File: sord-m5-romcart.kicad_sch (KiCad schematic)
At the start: 1 part

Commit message: Investigating banking
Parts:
- added U2: 27C256, Package_DIP:DIP-28_W15.24mm, symbol Memory_EPROM:27C256
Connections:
- net +5V: now also U2.28 (VCC)
- net GND: now also U2.1 (VPP), U2.14 (GND)
- net D1: now reaches U1.10 (D1)
- net D1: now also U2.12 (D1)
- net D0: now reaches U1.11 (D0)
- net D0: now also U2.11 (D0)
- net A7: now reaches U1.12 (A7)
- net A7: now also U2.3 (A7)
- net A6: now reaches U1.13 (A6)
- net A6: now also U2.4 (A6)
- net A5: now reaches U1.14 (A5)
- net A5: now also U2.5 (A5)
- net A4: now reaches U1.15 (A4)
- net A4: now also U2.6 (A4)
- net A3: now reaches U1.16 (A3)
- net A3: now also U2.7 (A3)
- net A2: now reaches U1.17 (A2)
- net A2: now also U2.8 (A2)
- net A1: now reaches U1.18 (A1)
- net A1: now also U2.9 (A1)
- net A0: now reaches U1.19 (A0)
- net A0: now also U2.10 (A0)
- net ~{ROM0}: now reaches U1.22 (~{ROM0})
- net ~{ROM0}: now also U2.20 (~{CE})
- net ~{MEM_RD}: now reaches U1.24 (~{MEM_RD})
- net ~{MEM_RD}: now also U2.22 (~{OE})
- net D4: now reaches U1.36 (D4)
- net D4: now also U2.16 (D4)
- net D5: now reaches U1.37 (D5)
- net D5: now also U2.17 (D5)
- net D6: now reaches U1.38 (D6)
- net D6: now also U2.18 (D6)
- net D7: now reaches U1.39 (D7)
- net D7: now also U2.19 (D7)
- net A8: now reaches U1.40 (A8)
- net A8: now also U2.25 (A8)
- net A9: now reaches U1.41 (A9)
- net A9: now also U2.24 (A9)
- net A10: now reaches U1.42 (A10)
- net A10: now also U2.21 (A10)
- net A11: now reaches U1.43 (A11)
- net A11: now also U2.23 (A11)
- net A12: now reaches U1.44 (A12)
- net D3: now reaches U1.8 (D3)
- net D3: now also U2.15 (D3)
- net D2: now reaches U1.9 (D2)
- net D2: now also U2.13 (D2)
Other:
- note added: "0x2000 (A13)"
- note added: "0x4000"
- note added: "0x6000"
- note added: "BASIC-{F,G,I,W}?"
- note added: "TODO: BASIC-G cartridge also needs RAM (http://www.retropc.net/mm/m5/basic-g-logic.html)"
- note added: "TODO: BASIC-G is 16K + RAM, BASIC-I is 8K"
- note added: "TODO: Do a table and figure out where each ROM select is at (add a 139?)"

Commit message: Fumbling
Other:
- note added: "0x4000 (A14)"
- note added: "0x6000 (A13 + A14, "only 4k")"
- note removed: "0x4000"
- note removed: "0x6000"
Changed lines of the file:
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@@
 	(text "0x2000 (A13)"
 		(exclude_from_sim no)
-		(at 122.555 67.31 0)
+		(at 116.205 67.31 0)
 		(effects
 			(font
 				(size 1.27 1.27)
 			)
+			(justify left)
 		)
 	)
-	(text "0x6000"
+	(text "0x6000 (A13 + A14, \"only 4k\")"
 		(exclude_from_sim no)
-		(at 119.38 72.39 0)
+		(at 116.205 72.39 0)
 		(effects
 			(font
 				(size 1.27 1.27)
 			)
+			(justify left)
 		)
 	)
@@
 		)
 	)
-	(text "0x4000"
+	(text "0x4000 (A14)"
 		(exclude_from_sim no)
-		(at 119.38 69.85 0)
+		(at 116.205 69.85 0)
 		(effects
 			(font
 				(size 1.27 1.27)
 			)
+			(justify left)
 		)
 	)

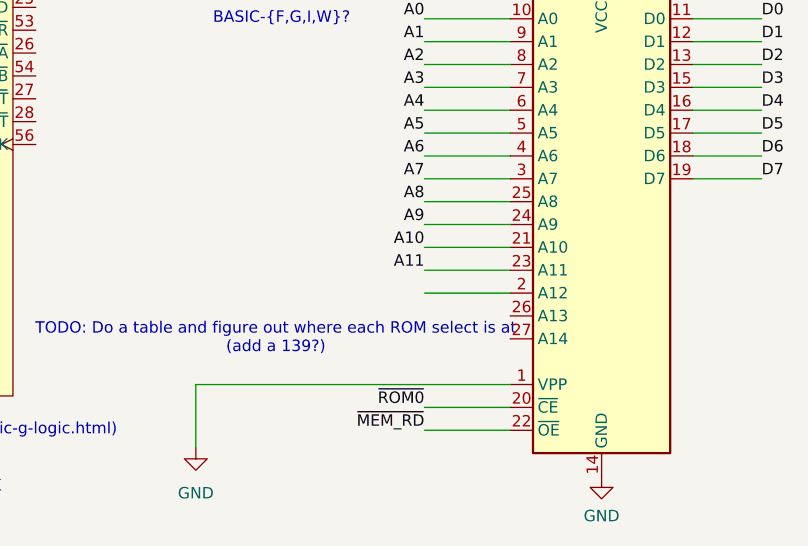
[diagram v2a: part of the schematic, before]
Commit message: A12 restored
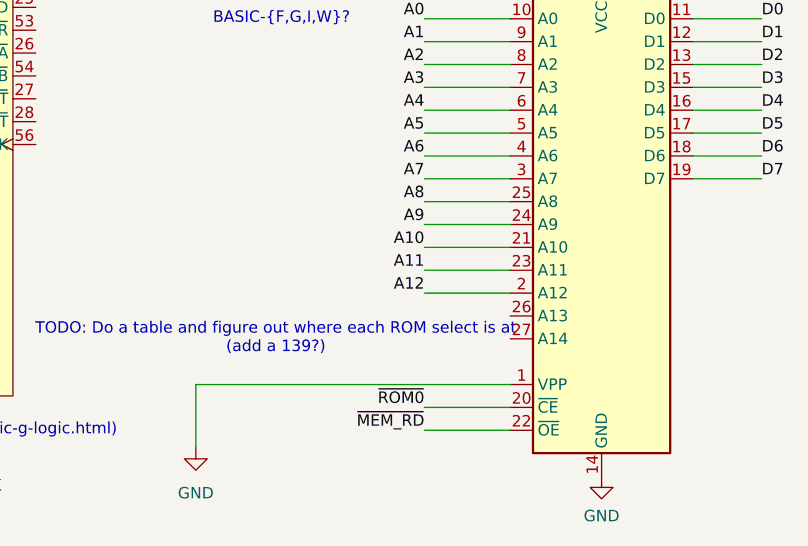
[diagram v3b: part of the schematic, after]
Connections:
- net A12: now also U2.2 (A12)
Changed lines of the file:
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@@
+		)
+	)
+	(label "A12"
+		(at 146.685 114.935 180)
+		(fields_autoplaced yes)
+		(effects
+			(font
+				(size 1.27 1.27)
+			)
+			(justify right bottom)
 		)
 	)

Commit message: Updated decode
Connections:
- net ~{ROM1}: now reaches U1.50 (~{ROM1})
- no-connect marks 0 -> 7
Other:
- note added: "TODO: decode the ROM0/ROM1 selects into high address lines"
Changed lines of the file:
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@@
 		(color 0 0 0 0)
 	)
+	(no_connect
+		(at 103.505 90.805)
+	)
+	(no_connect
+		(at 103.505 98.425)
+	)
+	(no_connect
+		(at 103.505 88.265)
+	)
+	(no_connect
+		(at 103.505 85.725)
+	)
+	(no_connect
+		(at 103.505 83.185)
+	)
+	(no_connect
+		(at 103.505 95.885)
+	)
+	(no_connect
+		(at 103.505 93.345)
+	)
 	(wire
 		(pts
@@
 		(pts
 			(xy 103.505 78.105) (xy 107.95 78.105)
+		)
+		(stroke
+			(width 0)
+			(type default)
+		)
+	)
+	(wire
+		(pts
+			(xy 103.505 70.485) (xy 107.95 70.485)
 		)
 		(stroke
@@
 		)
 	)
+	(text "TODO: decode the ROM0/ROM1 selects into high address lines"
+		(exclude_from_sim no)
+		(at 140.335 142.24 0)
+		(effects
+			(font
+				(size 1.27 1.27)
+			)
+		)
+	)
 	(label "A2"
 		(at 71.755 90.805 180)
@@
 		)
 	)
+	(label "~{ROM1}"
+		(at 107.95 70.485 0)
+		(fields_autoplaced yes)
+		(effects
+			(font
+				(size 1.27 1.27)
+			)
+			(justify left bottom)
+		)
+	)

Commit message: Board outline
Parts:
- U1: footprint (none) -> Sord:M5_CartridgeSlot
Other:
- note added: "TODO: Fix symbol pinout to be A/B"
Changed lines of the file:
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@@
+		)
+	)
+	(text "TODO: Fix symbol pinout to be A/B "
+		(exclude_from_sim no)
+		(at 76.835 144.78 0)
+		(effects
+			(font
+				(size 1.27 1.27)
+			)
 		)
 	)
@@
 			)
 		)
-		(property "Footprint" ""
+		(property "Footprint" "Sord:M5_CartridgeSlot"
 			(at 93.345 37.465 0)
 			(effects
@@
 			(at 93.345 37.465 0)
 			(effects
+				(font
+					(size 1.27 1.27)
+				)
+				(hide yes)
+			)
+		)
+		(property "DigiKey" ""
+			(at 93.345 37.465 0)
+			(effects

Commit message: Symbol cleanout
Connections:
- net +12V: now also U1.A2 (+12V_In), U1.A3 (+12V), U1.B2 (+12V_In), U1.B3 (+12V); no longer U1.2 (+12V_In), U1.3 (+12V), U1.30 (+12V_In), U1.31 (+12V)
- net +5V: now also U1.A4 (+5V_In), U1.A5 (+5V), U1.B4 (+5V_In), U1.B5 (+5V); no longer U1.32 (+5V_In), U1.33 (+5V), U1.4 (+5V_In), U1.5 (+5V)
- net -12V: now also U1.A1 (-12V), U1.B1 (-12V); no longer U1.1 (-12V), U1.29 (-12V)
- net A0: now also U1.A19 (A0); no longer U1.19 (A0)
- net A1: now also U1.A18 (A1); no longer U1.18 (A1)
- net A10: now also U1.B14 (A10); no longer U1.42 (A10)
- net A11: now also U1.B15 (A11); no longer U1.43 (A11)
- net A12: now also U1.B16 (A12); no longer U1.44 (A12)
- net A2: now also U1.A17 (A2); no longer U1.17 (A2)
- net A3: now also U1.A16 (A3); no longer U1.16 (A3)
- net A4: now also U1.A15 (A4); no longer U1.15 (A4)
- net A5: now also U1.A14 (A5); no longer U1.14 (A5)
- net A6: now also U1.A13 (A6); no longer U1.13 (A6)
- net A7: now also U1.A12 (A7); no longer U1.12 (A7)
- net A8: now also U1.B12 (A8); no longer U1.40 (A8)
- net A9: now also U1.B13 (A9); no longer U1.41 (A9)
- net D0: now also U1.A11 (D0); no longer U1.11 (D0)
- net D1: now also U1.A10 (D1); no longer U1.10 (D1)
- net D2: now also U1.A9 (D2); no longer U1.9 (D2)
- net D3: now also U1.A8 (D3); no longer U1.8 (D3)
- net D4: now also U1.B8 (D4); no longer U1.36 (D4)
- net D5: now also U1.B9 (D5); no longer U1.37 (D5)
- net D6: now also U1.B10 (D6); no longer U1.38 (D6)
- net D7: now also U1.B11 (D7); no longer U1.39 (D7)
- net GND: now also U1.A6 (GND), U1.A7 (GND), U1.B6 (GND), U1.B7 (GND); no longer U1.34 (GND), U1.35 (GND), U1.6 (GND), U1.7 (GND)
- net ~{MEM_RD}: now also U1.A24 (~{MEM_RD}); no longer U1.24 (~{MEM_RD})
- net ~{ROM0}: now also U1.A22 (~{ROM0}); no longer U1.22 (~{ROM0})
- net ~{ROM1}: now also U1.B22 (~{ROM1}); no longer U1.50 (~{ROM1})
- no-connect marks 7 -> 10
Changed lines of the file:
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@@
 	)
 	(no_connect
-		(at 103.505 98.425)
+		(at 103.505 100.965)
+	)
+	(no_connect
+		(at 103.505 103.505)
+	)
+	(no_connect
+		(at 103.505 108.585)
+	)
+	(no_connect
+		(at 103.505 106.045)
 	)
 	(no_connect
@@
 			)
 		)
-		(pin "1"
-		)
-		(pin "12"
-		)
-		(pin "13"
-		)
-		(pin "14"
-		)
-		(pin "15"
-		)
-		(pin "23"
-		)
-		(pin "24"
-		)
-		(pin "25"
-		)
-		(pin "26"
-		)
-		(pin "27"
-		)
-		(pin "10"
-		)
-		(pin "11"
-		)
-		(pin "28"
-		)
-		(pin "29"
-		)
-		(pin "3"
-		)
-		(pin "30"
-		)
-		(pin "31"
-		)
-		(pin "32"
-		)
-		(pin "33"
-		)
-		(pin "34"
-		)
-		(pin "2"
-		)
-		(pin "20"
-		)
-		(pin "21"
-		)
-		(pin "22"
-		)
-		(pin "16"
-		)
-		(pin "17"
-		)
-		(pin "18"
-		)
-		(pin "19"
-		)
-		(pin "35"
-		)
-		(pin "36"
-		)
-		(pin "37"
-		)
-		(pin "38"
-		)
-		(pin "39"
-		)
-		(pin "4"
-		)
-		(pin "40"
-		)
-		(pin "41"
-		)
-		(pin "42"
-		)
-		(pin "43"
-		)
-		(pin "44"
-		)
-		(pin "45"
-		)
-		(pin "46"
-		)
-		(pin "47"
-		)
-		(pin "5"
-		)
-		(pin "50"
-		)
-		(pin "51"
-		)
-		(pin "52"
-		)
-		(pin "53"
-		)
-		(pin "54"
-		)
-		(pin "56"
-		)
-		(pin "6"
-		)
-		(pin "7"
-		)
-		(pin "8"
-		)
-		(pin "9"
+		(pin "A20"
+		)
+		(pin "A21"
+		)
+		(pin "A22"
+		)
+		(pin "B22"
+		)
+		(pin "A23"
+		)
+		(pin "B23"
+		)
+		(pin "A24"
+		)
+		(pin "B24"
+		)
+		(pin "A25"
+		)
+		(pin "B25"
+		)
+		(pin "A26"
+		)
+		(pin "B26"
+		)
+		(pin "A27"
+		)
+		(pin "A28"
+		)
+		(pin "B27"
+		)
+		(pin "A8"
+		)
+		(pin "B8"
+		)
+		(pin "B9"
+		)
+		(pin "B10"
+		)
+		(pin "B11"
+		)
+		(pin "A19"
+		)
+		(pin "A18"
+		)
+		(pin "A17"
+		)
+		(pin "A16"
+		)
+		(pin "A15"
+		)
+		(pin "A14"
+		)
+		(pin "A13"
+		)
+		(pin "A12"
+		)
+		(pin "B12"
+		)
+		(pin "B13"
+		)
+		(pin "B14"
+		)
+		(pin "B15"
+		)
+		(pin "B16"
+		)
+		(pin "B17"
+		)
+		(pin "B18"
+		)
+		(pin "B19"
+		)
+		(pin "B1"
+		)
+		(pin "B2"
+		)
+		(pin "B3"
+		)
+		(pin "B4"
+		)
+		(pin "B5"
+		)
+		(pin "B6"
+		)
+		(pin "B7"
+		)
+		(pin "A1"
+		)
+		(pin "A2"
+		)
+		(pin "A3"
+		)
+		(pin "A4"
+		)
+		(pin "A5"
+		)
+		(pin "A6"
+		)
+		(pin "A7"
+		)
+		(pin "A11"
+		)
+		(pin "A10"
+		)
+		(pin "A9"
+		)
+		(pin "B28"
+		)
+		(pin "B20"
+		)
+		(pin "B21"
 		)
 		(instances

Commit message: V1 sent to fab
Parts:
- added R1: 10kΩ, Resistor_THT:R_Axial_DIN0207_L6.3mm_D2.5mm_P10.16mm_Horizontal, symbol Device:R_Small_US
- added SW1: Choose ROM, Connector_PinHeader_2.54mm:PinHeader_1x02_P2.54mm_Vertical, symbol Switch:SW_SPST
- added U3: 74LS00, Package_DIP:DIP-14_W7.62mm_Socket_LongPads, symbol 74xx:74LS00
- U2: footprint Package_DIP:DIP-28_W15.24mm -> Package_DIP:DIP-28_W15.24mm_Socket_LongPads
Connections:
- net +5V: now also SW1.1 (A), U3.14 (VCC)
- net GND: now also R1.2, U3.12, U3.13, U3.7 (GND)
- net ~{ROM0}: now also U3.1; no longer U2.20 (~{CE})
- net ~{ROM1}: now also U3.10, U3.2, U3.9
- net ROM_A13: now reaches U2.26 (A13)
- net ROM_A13: now also U3.8
- net ROM_A14: now reaches U2.27 (A14)
- net ROM_A14: now also R1.1, SW1.2 (B)
- net ~{ROM2}: now reaches U1.A23 (~{ROM2})
- new net: U3.3, U3.4, U3.5
- new net ~{ROM_CS}: U2.20 (~{CE}), U3.6
- no-connect marks 10 -> 11
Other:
- note added: "0x2000"
- note added: "0x4000"
- note added: "~{Select} = ~{ROM0} and ~{ROM1} ROM_A13 = invert ~{ROM1}"
